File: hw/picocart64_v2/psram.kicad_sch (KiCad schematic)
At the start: 14 parts, among them U1 W25Q128JVS, U2 W25Q128JVS, U3 W25Q128JVS, U4 W25Q128JVS, U5 W25Q128JVS, U6 W25Q128JVS, U9 SN74LVC138AQDRQ1

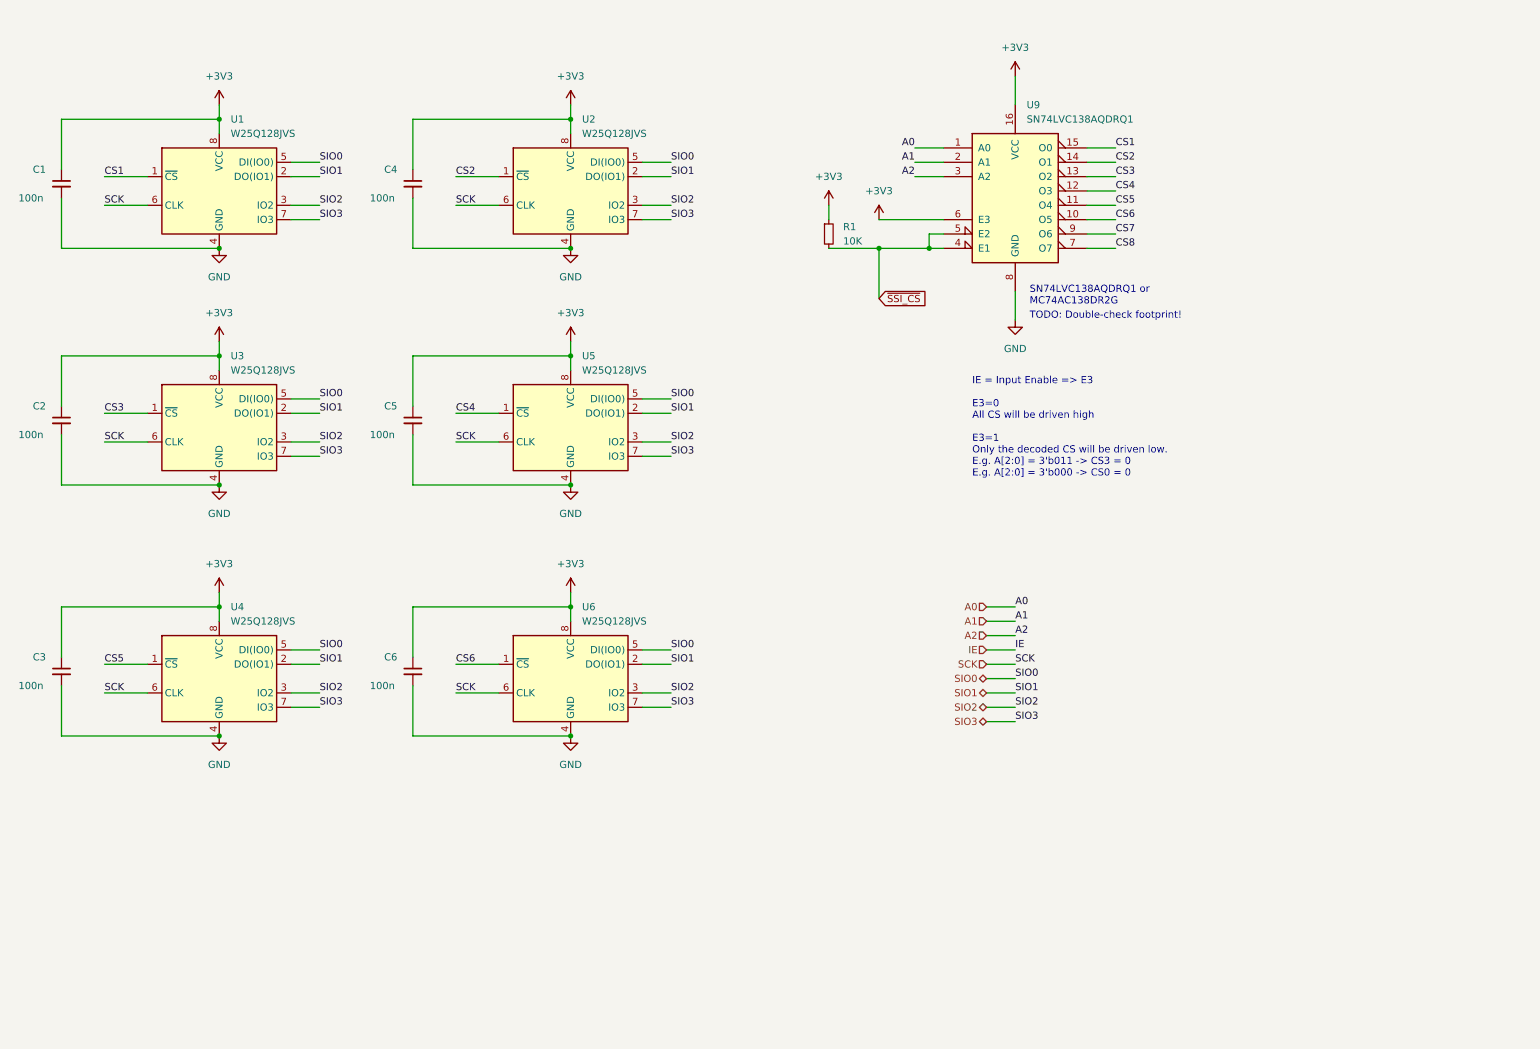
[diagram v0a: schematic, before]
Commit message: New v2 board revision (v2.2) updated with help from Snipeye. Updated readme.
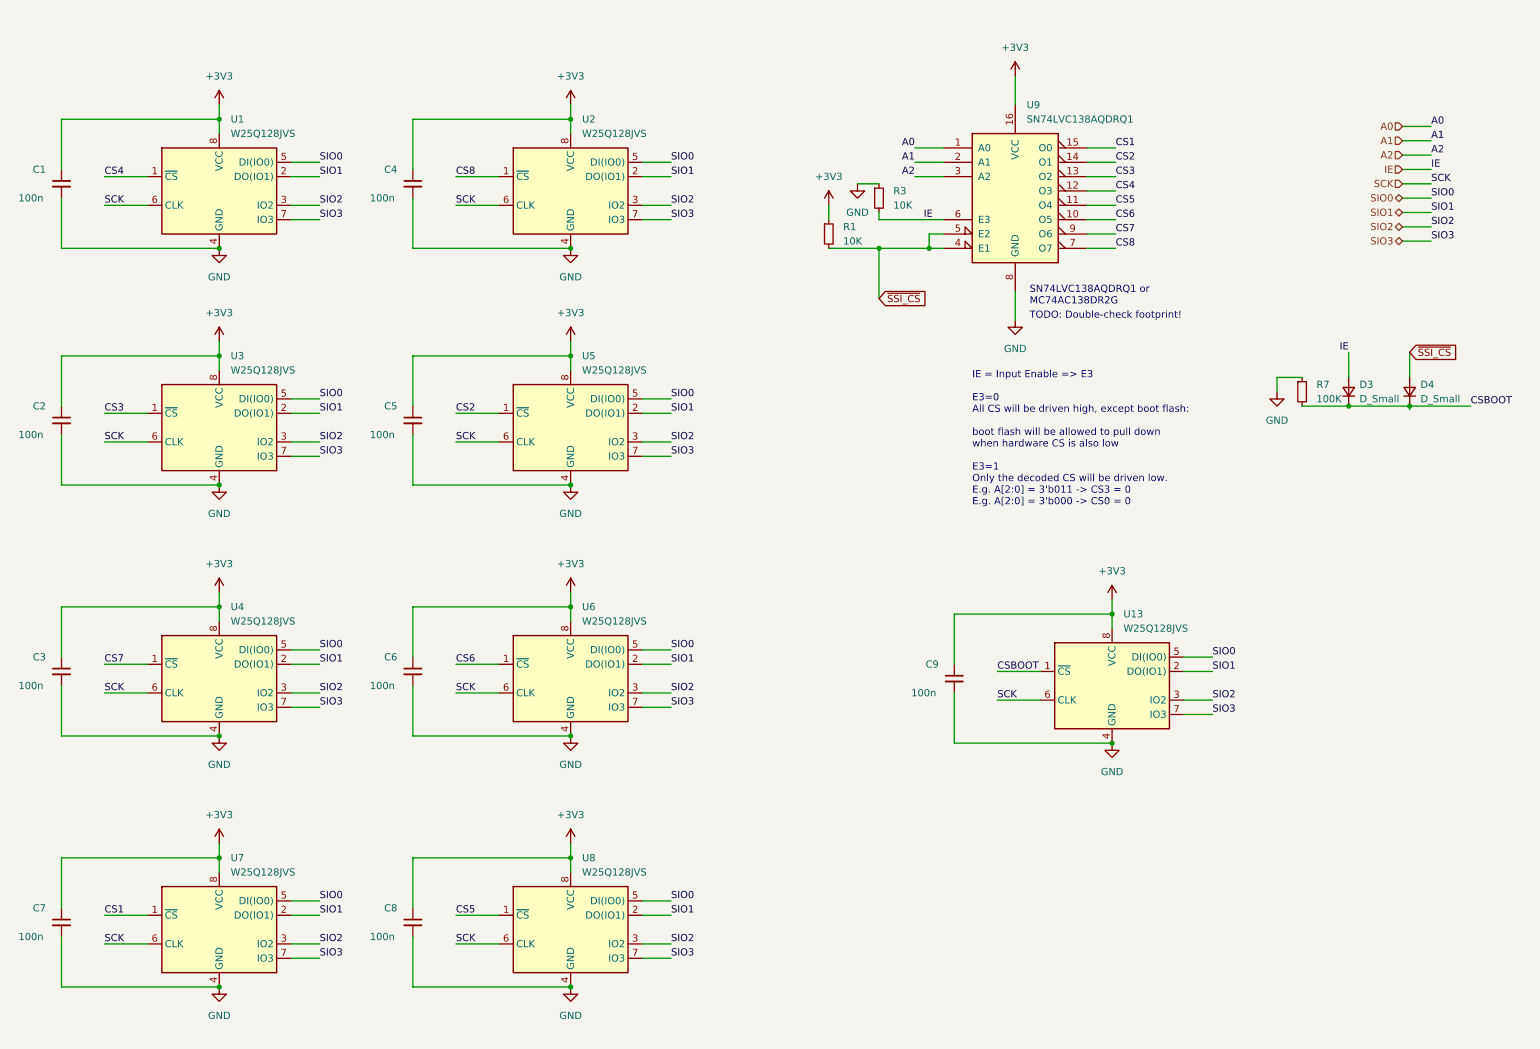
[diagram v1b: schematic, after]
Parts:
- added C7, C8, C9: 100n, Capacitor_SMD:C_0402_1005Metric, symbol Device:C_Small
- added D3, D4: D_Small, Diode_SMD:D_SOD-123, symbol Device:D_Small
- added R3: 10K, Resistor_SMD:R_0402_1005Metric, symbol Device:R_Small
- added R7: 100K, Resistor_SMD:R_0402_1005Metric, symbol Device:R_Small
- added U13, U7, U8: W25Q128JVS, Package_SO:SOIC-8_5.23x5.23mm_P1.27mm, symbol Memory_Flash:W25Q128JVS
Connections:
- net +3V3: now also C7.1, C8.1, C9.1, U13.8 (VCC), U7.8 (VCC), U8.8 (VCC); no longer U9.6 (E3)
- net CS1: now also U7.1 (~{CS}); no longer U1.1 (~{CS})
- net CS2: now also U5.1 (~{CS}); no longer U2.1 (~{CS})
- net CS4: now also U1.1 (~{CS}); no longer U5.1 (~{CS})
- net CS5: now also U8.1 (~{CS}); no longer U4.1 (~{CS})
- net CS7: now also U4.1 (~{CS})
- net CS8: now also U2.1 (~{CS})
- net GND: now also C7.2, C8.2, C9.2, R3.1, R7.1, U13.4 (GND), U7.4 (GND), U8.4 (GND)
- net IE: now also U9.6 (E3), D3.2 (A), R3.2
- net SCK: now also U13.6 (CLK), U7.6 (CLK), U8.6 (CLK)
- net SIO0: now also U13.5 (DI(IO0)), U7.5 (DI(IO0)), U8.5 (DI(IO0))
- net SIO1: now also U13.2 (DO(IO1)), U7.2 (DO(IO1)), U8.2 (DO(IO1))
- net SIO2: now also U13.3 (IO2), U7.3 (IO2), U8.3 (IO2)
- net SIO3: now also U13.7 (IO3), U7.7 (IO3), U8.7 (IO3)
- net ~{SSI_CS}: now also D4.2 (A)
- new net CSBOOT: D3.1 (K), D4.1 (K), R7.2, U13.1 (~{CS})
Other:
- note added: "IE = Input Enable => E3 E3=0 All CS will be driven high, except boot flash: boot flash will be allowed to pull down when hardware CS is also low E3=1 Only the decoded CS will be driven low. E.g. A[2:0] = 3'b011 -> CS3 = 0 E.g. A[2:0] = 3'b000 -> CS0 = 0"
- note removed: "IE = Input Enable => E3 E3=0 All CS will be driven high E3=1 Only the decoded CS will be driven low. E.g. A[2:0] = 3'b011 -> CS3 = 0 E.g. A[2:0] = 3'b000 -> CS0 = 0"

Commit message: Updated v2 pcb to use a tristate buffer to toggle between boot flash and psram array.
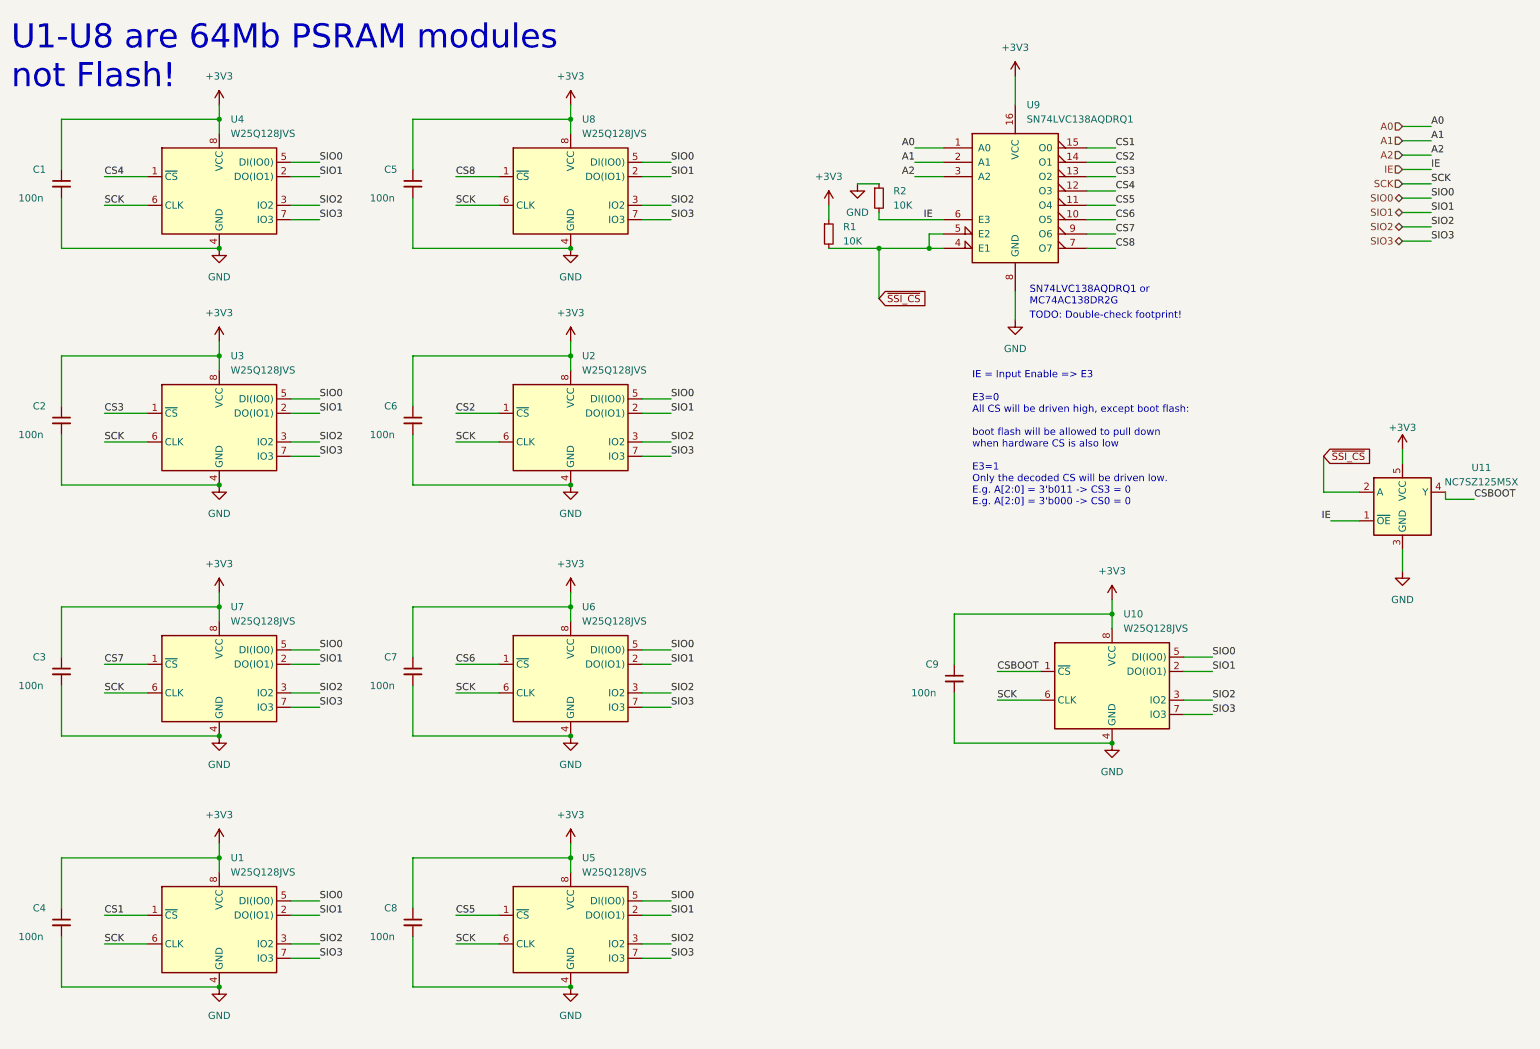
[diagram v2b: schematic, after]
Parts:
- removed D3, D4: D_Small, Diode_SMD:D_SOD-123, symbol Device:D_Small
- removed R7: 100K, Resistor_SMD:R_0402_1005Metric, symbol Device:R_Small
- added U11: NC7SZ125M5X, Package_TO_SOT_SMD:SOT-353_SC-70-5, symbol 74xGxx:NC7SZ125M5X
- renumbered C7 to C4, C4 to C5, C5 to C6, C6 to C7, R3 to R2, U7 to U1, U13 to U10, U5 to U2, U1 to U4, U8 to U5, U4 to U7, U2 to U8
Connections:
- net +3V3: now also U11.5 (VCC)
- net CSBOOT: now also U11.4 (Y)
- net GND: now also U11.3 (GND)
- net IE: now also U11.1 (~{OE})
- net ~{SSI_CS}: now also U11.2 (A)
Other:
- note added: "U1-U8 are 64Mb PSRAM modules not Flash!"

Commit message: Updated schematic to use correct footprints for the psram. Also updated the components and datasheets for the tristate buffer and psram.
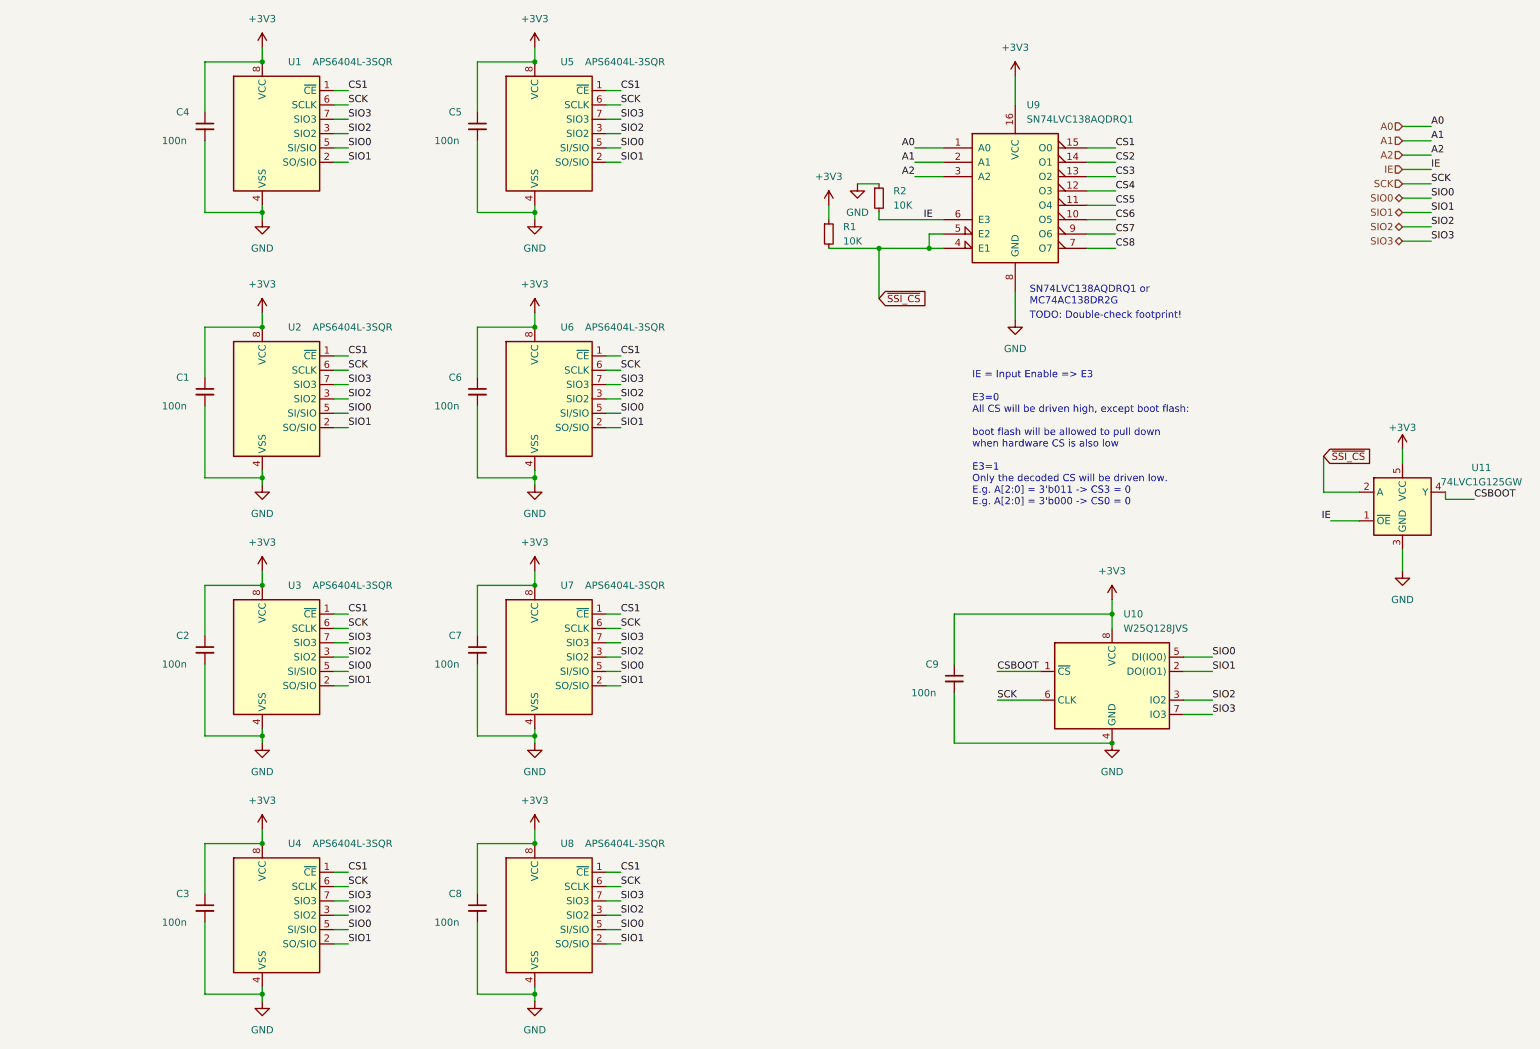
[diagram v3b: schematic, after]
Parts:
- removed U2, U3, U4, U5, U6, U7, U8: W25Q128JVS, Package_SO:SOIC-8_5.23x5.23mm_P1.27mm, symbol Memory_Flash:W25Q128JVS
- added U2, U3, U4, U5, U6, U7, U8: APS6404L-3SQR, Package_SO:SOP-8_3.76x4.96mm_P1.27mm, symbol Memory_RAM:ESP-PSRAM32
- U1: value W25Q128JVS -> APS6404L-3SQR; footprint Package_SO:SOIC-8_5.23x5.23mm_P1.27mm -> Package_SO:SOP-8_3.76x4.96mm_P1.27mm; symbol Memory_Flash:W25Q128JVS -> Memory_RAM:ESP-PSRAM32
- U11: value NC7SZ125M5X -> 74LVC1G125GW
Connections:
- net +3V3: now also U2.8 (VCC), U3.8 (VCC), U4.8 (VCC), U5.8 (VCC), U6.8 (VCC), U7.8 (VCC), U8.8 (VCC)
- net CS1: now also U2.1 (~{CE}), U3.1 (~{CE}), U4.1 (~{CE}), U5.1 (~{CE}), U6.1 (~{CE}), U7.1 (~{CE}), U8.1 (~{CE})
- net GND: now also U2.4 (VSS), U3.4 (VSS), U4.4 (VSS), U5.4 (VSS), U6.4 (VSS), U7.4 (VSS), U8.4 (VSS)
- net SCK: now also U2.6 (SCLK), U3.6 (SCLK), U4.6 (SCLK), U5.6 (SCLK), U6.6 (SCLK), U7.6 (SCLK), U8.6 (SCLK)
- net SIO0: now also U2.5 (SI/SIO), U3.5 (SI/SIO), U4.5 (SI/SIO), U5.5 (SI/SIO), U6.5 (SI/SIO), U7.5 (SI/SIO), U8.5 (SI/SIO)
- net SIO1: now also U2.2 (SO/SIO), U3.2 (SO/SIO), U4.2 (SO/SIO), U5.2 (SO/SIO), U6.2 (SO/SIO), U7.2 (SO/SIO), U8.2 (SO/SIO)
- net SIO2: now also U2.3 (SIO2), U3.3 (SIO2), U4.3 (SIO2), U5.3 (SIO2), U6.3 (SIO2), U7.3 (SIO2), U8.3 (SIO2)
- net SIO3: now also U2.7 (SIO3), U3.7 (SIO3), U4.7 (SIO3), U5.7 (SIO3), U6.7 (SIO3), U7.7 (SIO3), U8.7 (SIO3)
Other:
- note removed: "U1-U8 are 64Mb PSRAM modules not Flash!"
- moved on the sheet: C4, U1

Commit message: Updated hardware files
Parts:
- added C39, C40, C41, C42, C43, C44, C45, C46, C47: 1u, Capacitor_SMD:C_0402_1005Metric, symbol Device:C_Small
- added R62: 10K, Resistor_SMD:R_0402_1005Metric, symbol Device:R_Small
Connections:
- net +3V3: now also C39.1, C40.1, C41.1, C42.1, C43.1, C44.1, C45.1, C46.1, C47.1, R62.2
- net CS1: no longer U2.1 (~{CE}), U3.1 (~{CE}), U4.1 (~{CE}), U5.1 (~{CE}), U6.1 (~{CE}), U7.1 (~{CE}), U8.1 (~{CE})
- net CS2: now also U2.1 (~{CE})
- net CS3: now also U3.1 (~{CE})
- net CS4: now also U4.1 (~{CE})
- net CS5: now also U5.1 (~{CE})
- net CS6: now also U6.1 (~{CE})
- net CS7: now also U7.1 (~{CE})
- net CS8: now also U8.1 (~{CE})
- net CSBOOT: now also R62.1
- net GND: now also C39.2, C40.2, C41.2, C42.2, C43.2, C44.2, C45.2, C46.2, C47.2
